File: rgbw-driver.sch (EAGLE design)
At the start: 16 parts, among them J1 M20, J2 M20, Q1 IRLL014, Q2 IRLL014, Q3 IRLL014, Q4 IRLL014, X1 2PIN

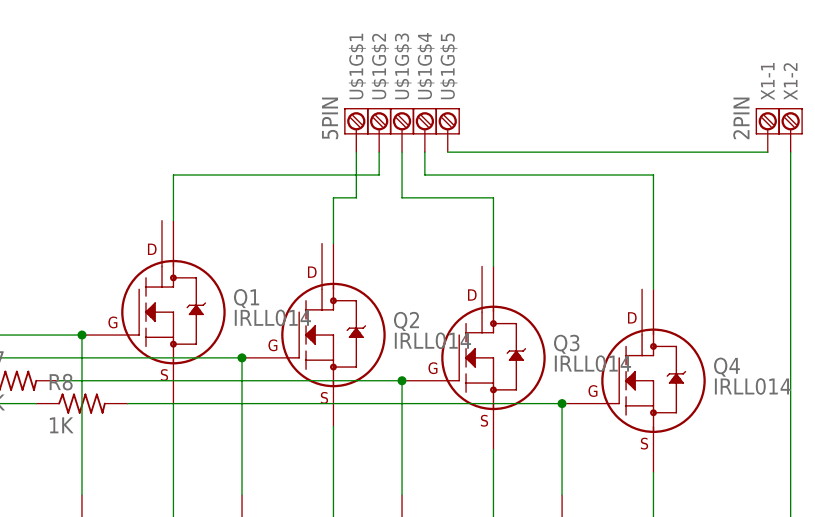
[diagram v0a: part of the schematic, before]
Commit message: RGBW traces now are polygonal pours for heat dissipation
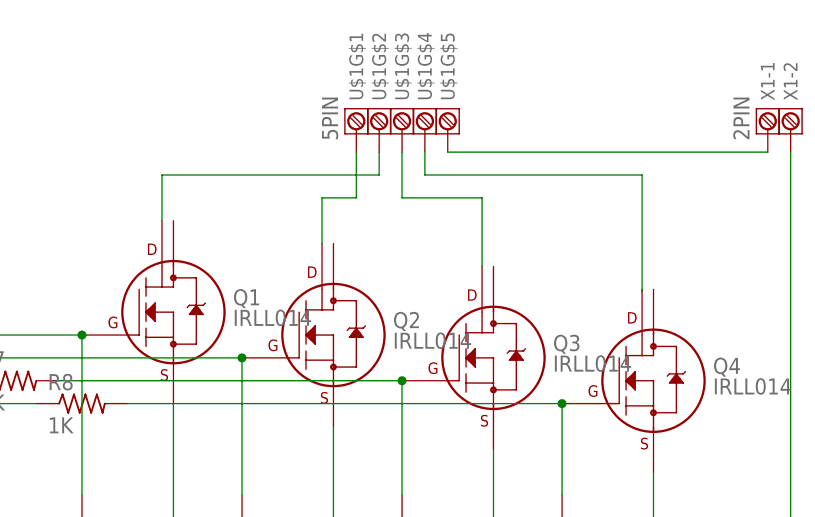
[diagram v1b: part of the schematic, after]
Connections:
- net N$31 renamed V+
- removed net N$50: Q1.D1, U$1G$2.1
- removed net N$51: Q2.D1, U$1G$1.1
- removed net N$52: Q3.D1, U$1G$3.1
- removed net N$53: Q4.D1, U$1G$4.1
- new net B: Q1.D2, U$1G$2.1
- new net G: U$1G$4.1
- new net R: Q3.D2, U$1G$3.1
- new net W: Q2.D2, U$1G$1.1
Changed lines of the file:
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@@
 </segment>
 </net>
-<net name="N$50" class="0">
+<net name="B" class="0">
 <segment>
-<pinref part="Q1" gate="G$1" pin="D1"/>
-<wire x1="167.64" y1="187.96" x2="167.64" y2="193.04" width="0.1524" layer="91"/>
-<wire x1="167.64" y1="193.04" x2="190.5" y2="193.04" width="0.1524" layer="91"/>
+<wire x1="166.37" y1="193.04" x2="190.5" y2="193.04" width="0.1524" layer="91"/>
 <pinref part="U$1" gate="G$2" pin="1"/>
 <wire x1="190.5" y1="193.04" x2="190.5" y2="195.58" width="0.1524" layer="91"/>
+<pinref part="Q1" gate="G$1" pin="D2"/>
+<wire x1="166.37" y1="193.04" x2="166.37" y2="187.96" width="0.1524" layer="91"/>
 </segment>
 </net>
-<net name="N$51" class="0">
+<net name="W" class="0">
 <segment>
-<pinref part="Q2" gate="G$1" pin="D1"/>
-<wire x1="185.42" y1="185.42" x2="185.42" y2="190.5" width="0.1524" layer="91"/>
-<wire x1="185.42" y1="190.5" x2="187.96" y2="190.5" width="0.1524" layer="91"/>
+<wire x1="184.15" y1="190.5" x2="187.96" y2="190.5" width="0.1524" layer="91"/>
 <pinref part="U$1" gate="G$1" pin="1"/>
 <wire x1="187.96" y1="195.58" x2="187.96" y2="190.5" width="0.1524" layer="91"/>
+<pinref part="Q2" gate="G$1" pin="D2"/>
+<wire x1="184.15" y1="190.5" x2="184.15" y2="185.42" width="0.1524" layer="91"/>
 </segment>
 </net>
-<net name="N$52" class="0">
+<net name="R" class="0">
 <segment>
 <pinref part="U$1" gate="G$3" pin="1"/>
 <wire x1="193.04" y1="195.58" x2="193.04" y2="190.5" width="0.1524" layer="91"/>
-<wire x1="193.04" y1="190.5" x2="203.2" y2="190.5" width="0.1524" layer="91"/>
-<pinref part="Q3" gate="G$1" pin="D1"/>
-<wire x1="203.2" y1="190.5" x2="203.2" y2="182.88" width="0.1524" layer="91"/>
+<wire x1="193.04" y1="190.5" x2="201.93" y2="190.5" width="0.1524" layer="91"/>
+<pinref part="Q3" gate="G$1" pin="D2"/>
+<wire x1="201.93" y1="190.5" x2="201.93" y2="182.88" width="0.1524" layer="91"/>
 </segment>
 </net>
-<net name="N$53" class="0">
+<net name="G" class="0">
 <segment>
-<pinref part="Q4" gate="G$1" pin="D1"/>
-<wire x1="220.98" y1="193.04" x2="220.98" y2="180.34" width="0.1524" layer="91"/>
 <pinref part="U$1" gate="G$4" pin="1"/>
 <wire x1="195.58" y1="195.58" x2="195.58" y2="193.04" width="0.1524" layer="91"/>
-<wire x1="195.58" y1="193.04" x2="220.98" y2="193.04" width="0.1524" layer="91"/>
+<wire x1="195.58" y1="193.04" x2="219.71" y2="193.04" width="0.1524" layer="91"/>
+<wire x1="219.71" y1="193.04" x2="219.71" y2="180.086" width="0.1524" layer="91"/>
 </segment>
 </net>
-<net name="N$31" class="0">
+<net name="V+" class="0">
 <segment>
 <pinref part="U$1" gate="G$5" pin="1"/>

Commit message: Minor schematic and silkscreen improvements
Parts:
- Q1, Q2, Q3, Q4: value IRLL014 -> STN4NF03L
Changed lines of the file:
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@@
 <part name="FRAME1" library="SparkFun3" deviceset="FRAME-A3" device=""/>
 <part name="R5" library="resistor" deviceset="R-US_" device="R0805" value="1K"/>
-<part name="Q1" library="transistors" deviceset="IRLL*" device="" technology="014"/>
+<part name="Q1" library="transistors" deviceset="IRLL*" device="" technology="014" value="STN4NF03L"/>
 <part name="R1" library="resistor" deviceset="R-US_" device="R0805" value="1M"/>
-<part name="Q2" library="transistors" deviceset="IRLL*" device="" technology="014"/>
-<part name="Q3" library="transistors" deviceset="IRLL*" device="" technology="014"/>
-<part name="Q4" library="transistors" deviceset="IRLL*" device="" technology="014"/>
+<part name="Q2" library="transistors" deviceset="IRLL*" device="" technology="014" value="STN4NF03L"/>
+<part name="Q3" library="transistors" deviceset="IRLL*" device="" technology="014" value="STN4NF03L"/>
+<part name="Q4" library="transistors" deviceset="IRLL*" device="" technology="014" value="STN4NF03L"/>
 <part name="R2" library="resistor" deviceset="R-US_" device="R0805" value="1M"/>
 <part name="R3" library="resistor" deviceset="R-US_" device="R0805" value="1M"/>

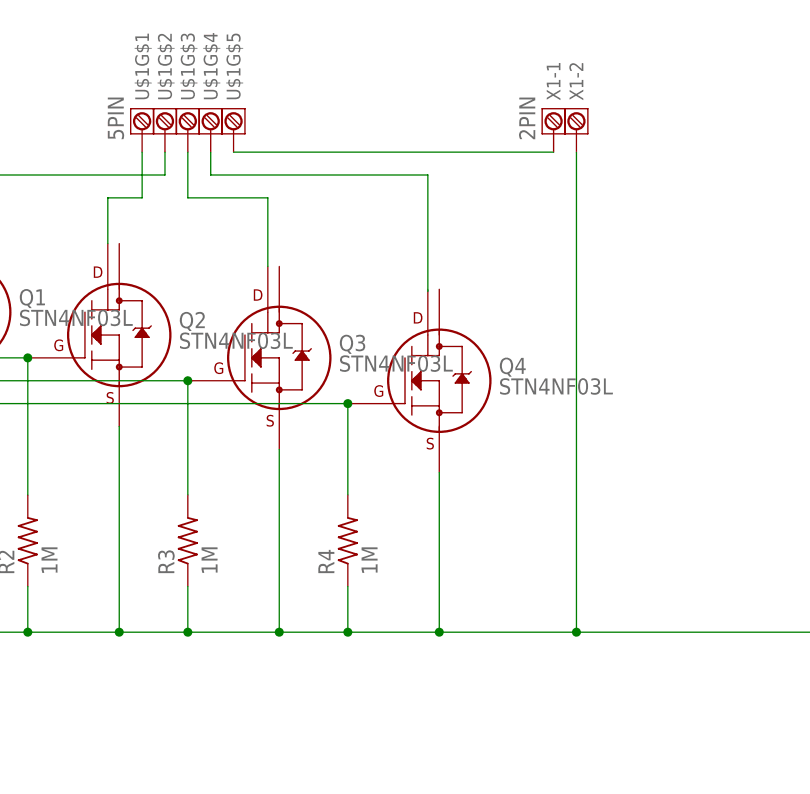
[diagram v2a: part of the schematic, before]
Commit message: Added power indicator LED
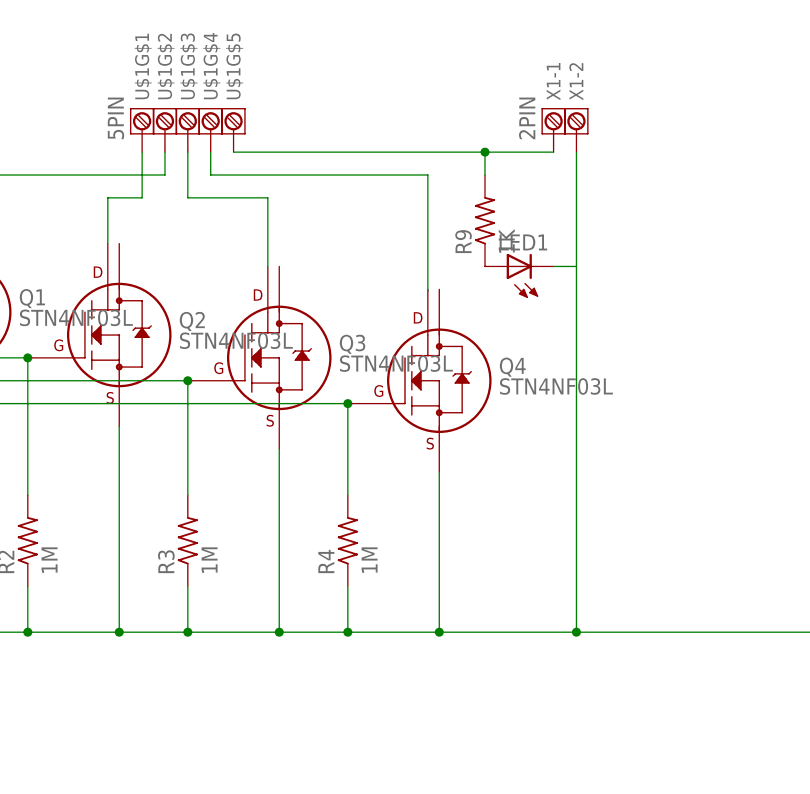
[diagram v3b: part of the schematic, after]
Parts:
- added LED1: (no value), adafruit:LEDCHIP-LED0805
- added R9: 1K, rcl:R-US_R0805
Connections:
- removed net V+: U$1G$5.1, X1-1.1
- new net N$3: LED1.A, R9.1
- new net N$6: R9.2, U$1G$5.1, X1-1.1
- net N$4: now also LED1.C
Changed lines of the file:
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@@
 <layer number="54" name="bGND_GNDA" color="1" fill="9" visible="no" active="no"/>
 <layer number="56" name="wert" color="7" fill="1" visible="no" active="no"/>
+<layer number="57" name="tCAD" color="7" fill="1" visible="no" active="no"/>
 <layer number="91" name="Nets" color="2" fill="1" visible="yes" active="yes"/>
 <layer number="92" name="Busses" color="1" fill="1" visible="yes" active="yes"/>
@@
 <layer number="97" name="Info" color="7" fill="1" visible="yes" active="yes"/>
 <layer number="98" name="Guide" color="6" fill="1" visible="yes" active="yes"/>
+<layer number="99" name="SpiceOrder" color="7" fill="1" visible="no" active="no"/>
 <layer number="100" name="Muster" color="7" fill="1" visible="no" active="no"/>
 <layer number="101" name="Patch_Top" color="12" fill="4" visible="yes" active="yes"/>
@@
 <layer number="106" name="bPlate" color="7" fill="1" visible="yes" active="yes"/>
 <layer number="107" name="Crop" color="7" fill="1" visible="yes" active="yes"/>
+<layer number="108" name="fp8" color="7" fill="1" visible="no" active="yes"/>
+<layer number="109" name="fp9" color="7" fill="1" visible="no" active="yes"/>
+<layer number="110" name="fp0" color="7" fill="1" visible="no" active="yes"/>
+<layer number="111" name="LPC17xx" color="7" fill="1" visible="no" active="yes"/>
+<layer number="112" name="tSilk" color="7" fill="1" visible="no" active="yes"/>
+<layer number="113" name="ReferenceLS" color="7" fill="1" visible="no" active="no"/>
 <layer number="116" name="Patch_BOT" color="9" fill="4" visible="yes" active="yes"/>
+<layer number="118" name="Rect_Pads" color="7" fill="1" visible="no" active="no"/>
 <layer number="121" name="_tsilk" color="7" fill="1" visible="yes" active="yes"/>
 <layer number="122" name="_bsilk" color="7" fill="1" visible="yes" active="yes"/>
+<layer number="123" name="tTestmark" color="7" fill="1" visible="no" active="yes"/>
+<layer number="124" name="bTestmark" color="7" fill="1" visible="no" active="yes"/>
+<layer number="125" name="_tNames" color="7" fill="1" visible="no" active="yes"/>
+<layer number="126" name="_bNames" color="7" fill="1" visible="no" active="yes"/>
+<layer number="127" name="_tValues" color="7" fill="1" visible="no" active="yes"/>
+<layer number="128" name="_bValues" color="7" fill="1" visible="no" active="yes"/>
+<layer number="131" name="tAdjust" color="7" fill="1" visible="no" active="yes"/>
+<layer number="132" name="bAdjust" color="7" fill="1" visible="no" active="yes"/>
+<layer number="144" name="Drill_legend" color="7" fill="1" visible="no" active="yes"/>
+<layer number="150" name="Notes" color="7" fill="1" visible="no" active="yes"/>
 <layer number="151" name="HeatSink" color="7" fill="1" visible="yes" active="yes"/>
+<layer number="152" name="_bDocu" color="7" fill="1" visible="no" active="yes"/>
+<layer number="153" name="FabDoc1" color="6" fill="1" visible="no" active="no"/>
+<layer number="154" name="FabDoc2" color="2" fill="1" visible="no" active="no"/>
+<layer number="155" name="FabDoc3" color="7" fill="15" visible="no" active="no"/>
 <layer number="199" name="Contour" color="7" fill="1" visible="no" active="yes"/>
 <layer number="200" name="200bmp" color="1" fill="10" visible="yes" active="yes"/>
@@
 <layer number="207" name="207bmp" color="8" fill="10" visible="yes" active="yes"/>
 <layer number="208" name="208bmp" color="9" fill="10" visible="yes" active="yes"/>
+<layer number="209" name="209bmp" color="7" fill="1" visible="no" active="yes"/>
+<layer number="210" name="210bmp" color="7" fill="1" visible="no" active="yes"/>
+<layer number="211" name="211bmp" color="7" fill="1" visible="no" active="yes"/>
+<layer number="212" name="212bmp" color="7" fill="1" visible="no" active="yes"/>
+<layer number="213" name="213bmp" color="7" fill="1" visible="no" active="yes"/>
+<layer number="214" name="214bmp" color="7" fill="1" visible="no" active="yes"/>
+<layer number="215" name="215bmp" color="7" fill="1" visible="no" active="yes"/>
+<layer number="216" name="216bmp" color="7" fill="1" visible="no" active="yes"/>
+<layer number="217" name="217bmp" color="18" fill="1" visible="no" active="no"/>
+<layer number="218" name="218bmp" color="19" fill="1" visible="no" active="no"/>
+<layer number="219" name="219bmp" color="20" fill="1" visible="no" active="no"/>
+<layer number="220" name="220bmp" color="21" fill="1" visible="no" active="no"/>
+<layer number="221" name="221bmp" color="22" fill="1" visible="no" active="no"/>
+<layer number="222" name="222bmp" color="23" fill="1" visible="no" active="no"/>
+<layer number="223" name="223bmp" color="24" fill="1" visible="no" active="no"/>
+<layer number="224" name="224bmp" color="25" fill="1" visible="no" active="no"/>
+<layer number="231" name="Eagle3D_PG1" color="7" fill="1" visible="no" active="no"/>
+<layer number="232" name="Eagle3D_PG2" color="7" fill="1" visible="no" active="no"/>
+<layer number="233" name="Eagle3D_PG3" color="7" fill="1" visible="no" active="no"/>
+<layer number="248" name="Housing" color="7" fill="1" visible="no" active="yes"/>
+<layer number="249" name="Edge" color="7" fill="1" visible="no" active="yes"/>
 <layer number="250" name="Descript" color="3" fill="1" visible="no" active="no"/>
 <layer number="251" name="SMDround" color="12" fill="11" visible="no" active="no"/>
@@
 <part name="U$1" library="con-3.81" deviceset="5PIN" device=""/>
 <part name="X1" library="con-3.81" deviceset="2PIN" device=""/>
+<part name="R9" library="rcl" deviceset="R-US_" device="R0805" value="1K"/>
+<part name="LED1" library="adafruit" deviceset="LED" device="CHIP-LED0805"/>
 </parts>
 <sheets>
@@
 <instance part="X1" gate="-1" x="233.68" y="198.12" rot="MR270"/>
 <instance part="X1" gate="-2" x="236.22" y="198.12" rot="MR270"/>
+<instance part="R9" gate="G$1" x="226.06" y="187.96" rot="R90"/>
+<instance part="LED1" gate="G$1" x="228.6" y="182.88" rot="R90"/>
 </instances>
 <busses>
@@
 <junction x="220.98" y="142.24"/>
 <pinref part="X1" gate="-2" pin="1"/>
-<wire x1="236.22" y1="195.58" x2="236.22" y2="142.24" width="0.1524" layer="91"/>
+<wire x1="236.22" y1="195.58" x2="236.22" y2="182.88" width="0.1524" layer="91"/>
 <junction x="236.22" y="142.24"/>
+<pinref part="LED1" gate="G$1" pin="C"/>
+<wire x1="236.22" y1="182.88" x2="236.22" y2="142.24" width="0.1524" layer="91"/>
+<wire x1="233.68" y1="182.88" x2="236.22" y2="182.88" width="0.1524" layer="91"/>
 </segment>
 </net>
@@
 </segment>
 </net>
-<net name="V+" class="0">
+<net name="N$3" class="0">
+<segment>
+<pinref part="R9" gate="G$1" pin="1"/>
+<pinref part="LED1" gate="G$1" pin="A"/>
+</segment>
+</net>
+<net name="N$6" class="0">
 <segment>
 <pinref part="U$1" gate="G$5" pin="1"/>
 <pinref part="X1" gate="-1" pin="1"/>
-<wire x1="198.12" y1="195.58" x2="233.68" y2="195.58" width="0.1524" layer="91"/>
-</segment>
-</net>
+<wire x1="198.12" y1="195.58" x2="226.06" y2="195.58" width="0.1524" layer="91"/>
+<pinref part="R9" gate="G$1" pin="2"/>
+<wire x1="226.06" y1="195.58" x2="233.68" y2="195.58" width="0.1524" layer="91"/>
+<wire x1="226.06" y1="195.58" x2="226.06" y2="193.04" width="0.1524" layer="91"/>
+<junction x="226.06" y="195.58"/>
+</segment>
+</net>
